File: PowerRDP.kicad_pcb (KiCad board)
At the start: 2 copper layers, 72.6 x 46.7 mm, 55 parts, among them J1 Conn_01x02_Male, J10 FPGA, J11 FAA LED, J12 Switch, J13 Conn_Coaxial, J14 Conn_Coaxial, J15 Conn_Coaxial, J2 Conn_01x02_Male, J3 Conn_01x02_Male, J4 Conn_01x02_Male, J5 Conn_01x02_Male, J6 Conn_01x02_Male, J7 3.3V, J8 5V, J9 12V, Q1 NTR4003NT1G, U1 Recom_RS3, U2 LM2575-3.3BU, U3 LM2575-5.0BU, U4 LM2575-12BU, U5 TS555, U6 MCP602, U7 MCP602

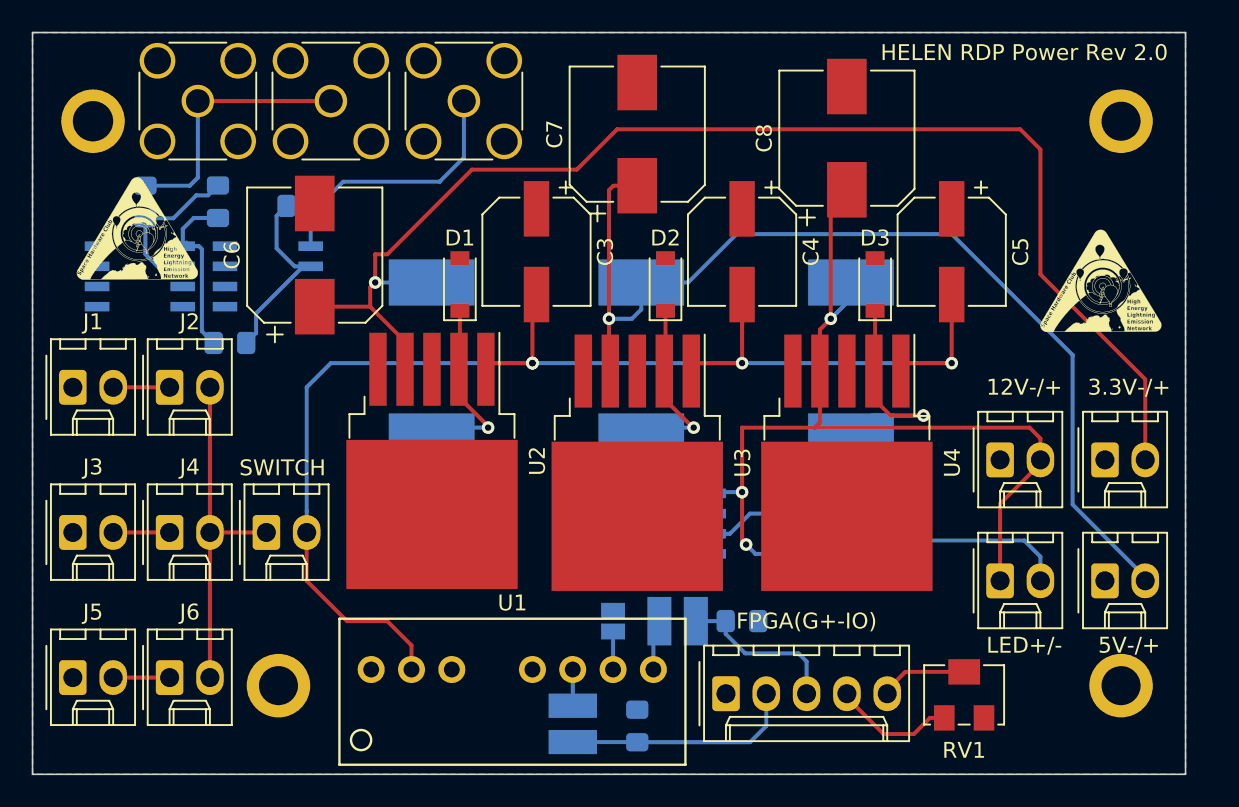
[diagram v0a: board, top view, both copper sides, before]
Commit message: Change R3 to through-hole for easier changes of amplification
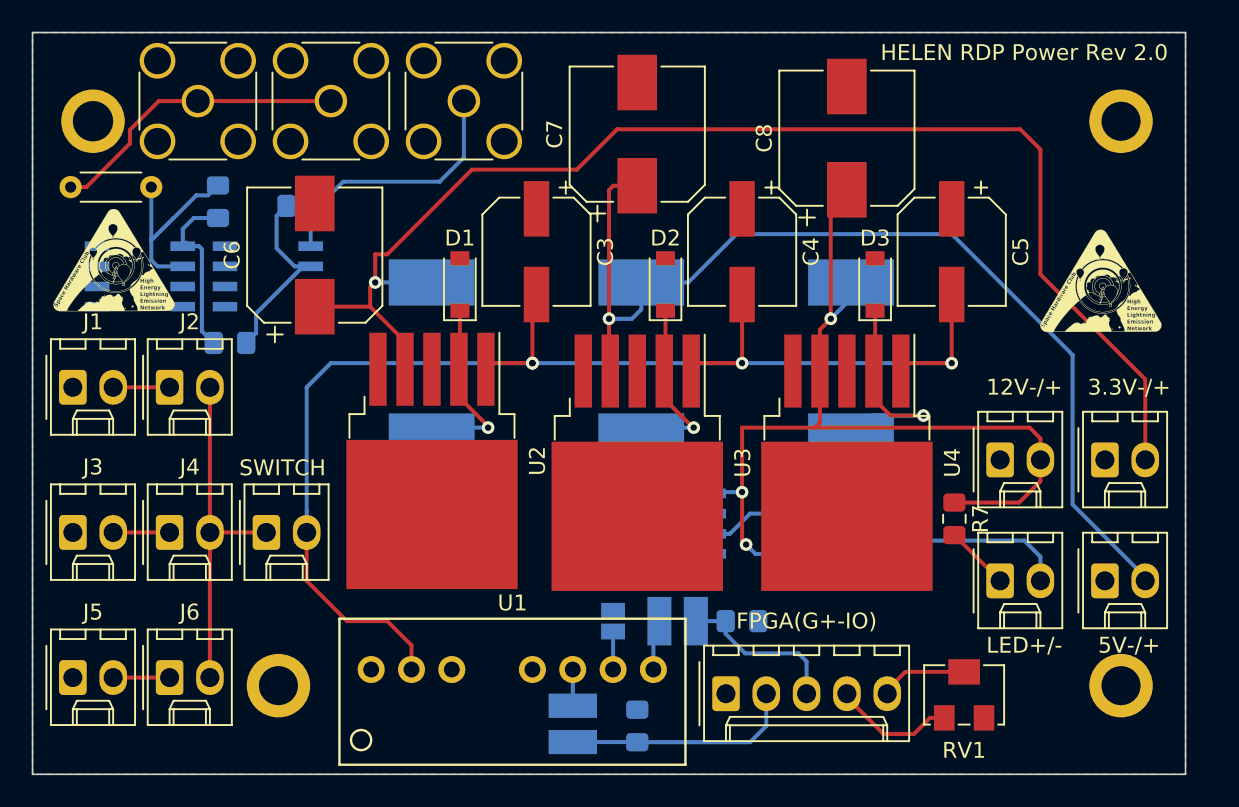
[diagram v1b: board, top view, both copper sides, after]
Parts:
- added R7: 15, Resistor_SMD:R_0805_2012Metric_Pad1.15x1.40mm_HandSolder, F.Cu at (141.9, 75.8)
- J10: value FPGA -> SOCKET
- R3: footprint Resistor_SMD:R_0805_2012Metric_Pad1.15x1.40mm_HandSolder -> Resistor_THT:R_Axial_DIN0204_L3.6mm_D1.6mm_P5.08mm_Horizontal; moved to F.Cu
- moved G*** 2.48 mm to (89.0, 59.4)
- moved R3 1.01 mm to (91.3, 55.0), turned to 180 degrees
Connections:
- J11 pad 1: /+12V -> Net-(J11-Pad1)
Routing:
- net Net-(J11-Pad1): track 0.00 -> 4.07 mm
- net /ADC1: track 16.7 -> 19.1 mm
- net Net-(R3-Pad1): track 11.1 -> 12.4 mm
- net /+12V: track 71.5 -> 70.4 mm

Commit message: Fix opamps
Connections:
- U6 pad 1: Net-(R4-Pad1) -> Net-(U6-Pad1)
- U6 pad 4: (no net) -> GND
- U6 pad 5: (no net) -> Net-(U6-Pad5)
- U6 pad 6: (no net) -> Net-(R4-Pad1)
- U6 pad 7: (no net) -> /+3.3V
- U6 pad 8: (no net) -> Net-(U6-Pad8)
- U7 pad 1: /ADC2 -> Net-(U7-Pad1)
- U7 pad 4: (no net) -> GND
- U7 pad 5: (no net) -> Net-(U7-Pad5)
- U7 pad 6: (no net) -> /ADC2
- U7 pad 7: (no net) -> /+3.3V
- U7 pad 8: (no net) -> Net-(U7-Pad8)
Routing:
- net /+3.3V: track 83.3 -> 103.0 mm, vias 1 -> 3
- net Net-(R4-Pad1): track 11.8 -> 25.1 mm, vias 0 -> 2
- net /ADC2: track 16.7 -> 27.6 mm
- net Net-(R3-Pad1): track 12.4 -> 11.4 mm
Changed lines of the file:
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@@
     (thickness 1.6)
     (drawings 24)
-    (tracks 209)
+    (tracks 231)
     (zones 0)
     (modules 56)
-    (nets 33)
+    (nets 39)
   )
   (page A4)
@@
   (net 31 "Net-(R5-Pad1)")
   (net 32 "Net-(J11-Pad1)")
+  (net 33 "Net-(U6-Pad8)")
+  (net 34 "Net-(U6-Pad5)")
+  (net 35 "Net-(U6-Pad1)")
+  (net 36 "Net-(U7-Pad1)")
+  (net 37 "Net-(U7-Pad5)")
+  (net 38 "Net-(U7-Pad8)")
   (net_class Default "This is the default net class."
     (clearance 0.2)
@@
     (add_net "Net-(U1-Pad3)")
     (add_net "Net-(U1-Pad5)")
+    (add_net "Net-(U6-Pad1)")
+    (add_net "Net-(U6-Pad5)")
+    (add_net "Net-(U6-Pad8)")
+    (add_net "Net-(U7-Pad1)")
+    (add_net "Net-(U7-Pad5)")
+    (add_net "Net-(U7-Pad8)")
   )
   (module rdplibs:HELENlogo_large (layer F.Cu)
@@
       (effects (font (size 1 1) (thickness 0.15)) (justify mirror))
     )
-    (pad 8 smd rect (at 2.7 1.905 180) (size 1.55 0.6) (layers B.Cu B.Paste B.Mask))
-    (pad 7 smd rect (at 2.7 0.635 180) (size 1.55 0.6) (layers B.Cu B.Paste B.Mask))
-    (pad 6 smd rect (at 2.7 -0.635 180) (size 1.55 0.6) (layers B.Cu B.Paste B.Mask))
-    (pad 5 smd rect (at 2.7 -1.905 180) (size 1.55 0.6) (layers B.Cu B.Paste B.Mask))
-    (pad 4 smd rect (at -2.7 -1.905 180) (size 1.55 0.6) (layers B.Cu B.Paste B.Mask))
+    (pad 8 smd rect (at 2.7 1.905 180) (size 1.55 0.6) (layers B.Cu B.Paste B.Mask)
+      (net 33 "Net-(U6-Pad8)"))
+    (pad 7 smd rect (at 2.7 0.635 180) (size 1.55 0.6) (layers B.Cu B.Paste B.Mask)
+      (net 5 /+3.3V))
+    (pad 6 smd rect (at 2.7 -0.635 180) (size 1.55 0.6) (layers B.Cu B.Paste B.Mask)
+      (net 30 "Net-(R4-Pad1)"))
+    (pad 5 smd rect (at 2.7 -1.905 180) (size 1.55 0.6) (layers B.Cu B.Paste B.Mask)
+      (net 34 "Net-(U6-Pad5)"))
+    (pad 4 smd rect (at -2.7 -1.905 180) (size 1.55 0.6) (layers B.Cu B.Paste B.Mask)
+      (net 2 GND))
     (pad 3 smd rect (at -2.7 -0.635 180) (size 1.55 0.6) (layers B.Cu B.Paste B.Mask)
       (net 2 GND))
@@
       (net 29 "Net-(R3-Pad1)"))
     (pad 1 smd rect (at -2.7 1.905 180) (size 1.55 0.6) (layers B.Cu B.Paste B.Mask)
-      (net 30 "Net-(R4-Pad1)"))
+      (net 35 "Net-(U6-Pad1)"))
     (model ${KISYS3DMOD}/Package_SO.3dshapes/SOIC-8_3.9x4.9mm_P1.27mm.wrl
       (at (xyz 0 0 0))
@@
     (fp_line (start -2.075 2.525) (end -3.475 2.525) (layer B.SilkS) (width 0.15))
     (pad 1 smd rect (at -2.7 1.905 180) (size 1.55 0.6) (layers B.Cu B.Paste B.Mask)
-      (net 28 /ADC2))
+      (net 36 "Net-(U7-Pad1)"))
     (pad 2 smd rect (at -2.7 0.635 180) (size 1.55 0.6) (layers B.Cu B.Paste B.Mask)
       (net 31 "Net-(R5-Pad1)"))
     (pad 3 smd rect (at -2.7 -0.635 180) (size 1.55 0.6) (layers B.Cu B.Paste B.Mask)
       (net 2 GND))
-    (pad 4 smd rect (at -2.7 -1.905 180) (size 1.55 0.6) (layers B.Cu B.Paste B.Mask))
-    (pad 5 smd rect (at 2.7 -1.905 180) (size 1.55 0.6) (layers B.Cu B.Paste B.Mask))
-    (pad 6 smd rect (at 2.7 -0.635 180) (size 1.55 0.6) (layers B.Cu B.Paste B.Mask))
-    (pad 7 smd rect (at 2.7 0.635 180) (size 1.55 0.6) (layers B.Cu B.Paste B.Mask))
-    (pad 8 smd rect (at 2.7 1.905 180) (size 1.55 0.6) (layers B.Cu B.Paste B.Mask))
+    (pad 4 smd rect (at -2.7 -1.905 180) (size 1.55 0.6) (layers B.Cu B.Paste B.Mask)
+      (net 2 GND))
+    (pad 5 smd rect (at 2.7 -1.905 180) (size 1.55 0.6) (layers B.Cu B.Paste B.Mask)
+      (net 37 "Net-(U7-Pad5)"))
+    (pad 6 smd rect (at 2.7 -0.635 180) (size 1.55 0.6) (layers B.Cu B.Paste B.Mask)
+      (net 28 /ADC2))
+    (pad 7 smd rect (at 2.7 0.635 180) (size 1.55 0.6) (layers B.Cu B.Paste B.Mask)
+      (net 5 /+3.3V))
+    (pad 8 smd rect (at 2.7 1.905 180) (size 1.55 0.6) (layers B.Cu B.Paste B.Mask)
+      (net 38 "Net-(U7-Pad8)"))
     (model ${KISYS3DMOD}/Package_SO.3dshapes/SOIC-8_3.9x4.9mm_P1.27mm.wrl
       (at (xyz 0 0 0))
@@
   (segment (start 120.65 51.308) (end 146.05 51.308) (width 0.25) (layer F.Cu) (net 5))
   (segment (start 118.11 53.848) (end 120.65 51.308) (width 0.25) (layer F.Cu) (net 5))
+  (via (at 97.79 59.944) (size 0.8) (drill 0.4) (layers F.Cu B.Cu) (net 5))
+  (segment (start 101.6 62.484) (end 101.6 61.984) (width 0.25) (layer F.Cu) (net 5))
+  (segment (start 99.56 59.944) (end 97.79 59.944) (width 0.25) (layer F.Cu) (net 5))
+  (segment (start 101.6 61.984) (end 99.56 59.944) (width 0.25) (layer F.Cu) (net 5))
+  (segment (start 97.79 59.944) (end 95.946 59.944) (width 0.25) (layer B.Cu) (net 5))
+  (segment (start 97.79 59.944) (end 93.218 59.944) (width 0.25) (layer F.Cu) (net 5))
+  (via (at 90.424 57.15) (size 0.8) (drill 0.4) (layers F.Cu B.Cu) (net 5))
+  (segment (start 93.218 59.944) (end 90.424 57.15) (width 0.25) (layer F.Cu) (net 5))
+  (segment (start 88.359 59.944) (end 87.884 59.944) (width 0.25) (layer B.Cu) (net 5))
+  (segment (start 90.424 57.879) (end 88.359 59.944) (width 0.25) (layer B.Cu) (net 5))
+  (segment (start 90.424 57.15) (end 90.424 57.879) (width 0.25) (layer B.Cu) (net 5))
   (segment (start 120.22 66.542) (end 120.22 68.292) (width 0.25) (layer F.Cu) (net 6))
   (via (at 120.142 63.246) (size 0.8) (drill 0.4) (layers F.Cu B.Cu) (net 6))
@@
   (segment (start 87.209949 54.95) (end 86.22 54.95) (width 0.25) (layer F.Cu) (net 27))
   (segment (start 91.77 49.53) (end 89.955001 51.344999) (width 0.25) (layer F.Cu) (net 27))
-  (segment (start 101.346 56.66) (end 101.872 56.134) (width 0.25) (layer B.Cu) (net 28))
-  (segment (start 101.346 58.674) (end 101.346 56.66) (width 0.25) (layer B.Cu) (net 28))
   (segment (start 103.396 54.61) (end 101.872 56.134) (width 0.25) (layer B.Cu) (net 28))
   (segment (start 109.474 54.61) (end 103.396 54.61) (width 0.25) (layer B.Cu) (net 28))
   (segment (start 110.998 49.53) (end 110.998 53.086) (width 0.25) (layer B.Cu) (net 28))
   (segment (start 110.998 53.086) (end 109.474 54.61) (width 0.25) (layer B.Cu) (net 28))
+  (segment (start 100.094 54.356) (end 101.872 56.134) (width 0.25) (layer B.Cu) (net 28))
+  (segment (start 98.552 54.356) (end 100.094 54.356) (width 0.25) (layer B.Cu) (net 28))
+  (segment (start 98.044 61.214) (end 98.806 60.452) (width 0.25) (layer B.Cu) (net 28))
+  (segment (start 98.298 54.61) (end 98.552 54.356) (width 0.25) (layer B.Cu) (net 28))
+  (segment (start 95.946 61.214) (end 98.044 61.214) (width 0.25) (layer B.Cu) (net 28))
+  (segment (start 98.806 60.452) (end 98.806 59.69) (width 0.25) (layer B.Cu) (net 28))
+  (segment (start 98.806 59.69) (end 98.298 59.182) (width 0.25) (layer B.Cu) (net 28))
+  (segment (start 98.298 59.182) (end 98.298 54.61) (width 0.25) (layer B.Cu) (net 28))
   (segment (start 94.880628 55.469372) (end 94.136628 55.469372) (width 0.25) (layer B.Cu) (net 29))
   (segment (start 95.504 54.846) (end 94.880628 55.469372) (width 0.25) (layer B.Cu) (net 29))
-  (segment (start 94.136628 55.469372) (end 92.692 56.914) (width 0.25) (layer B.Cu) (net 29))
   (segment (start 91.694 59.944) (end 93.284 59.944) (width 0.25) (layer B.Cu) (net 29))
   (segment (start 91.3 59.55) (end 91.694 59.944) (width 0.25) (layer B.Cu) (net 29))
-  (segment (start 92.686 56.914) (end 91.3 58.3) (width 0.25) (layer B.Cu) (net 29))
-  (segment (start 92.692 56.914) (end 92.686 56.914) (width 0.25) (layer B.Cu) (net 29))
   (segment (start 91.3 54.95) (end 91.3 58.3) (width 0.25) (layer B.Cu) (net 29))
   (segment (start 91.3 58.3) (end 91.3 59.55) (width 0.25) (layer B.Cu) (net 29))
-  (segment (start 93.52 58.438) (end 93.284 58.674) (width 0.25) (layer B.Cu) (net 30))
+  (segment (start 93.617256 54.95) (end 91.3 54.95) (width 0.25) (layer B.Cu) (net 29))
+  (segment (start 94.136628 55.469372) (end 93.617256 54.95) (width 0.25) (layer B.Cu) (net 29))
   (segment (start 95.504 64.498) (end 95.232 64.77) (width 0.25) (layer B.Cu) (net 30))
-  (segment (start 93.284 57.592) (end 93.284 58.674) (width 0.25) (layer B.Cu) (net 30))
   (segment (start 95.504 56.896) (end 93.98 56.896) (width 0.25) (layer B.Cu) (net 30))
-  (segment (start 93.98 56.896) (end 93.284 57.592) (width 0.25) (layer B.Cu) (net 30))
-  (segment (start 94.309 58.674) (end 94.488 58.853) (width 0.25) (layer B.Cu) (net 30))
-  (segment (start 93.284 58.674) (end 94.309 58.674) (width 0.25) (layer B.Cu) (net 30))
-  (segment (start 94.488 64.026) (end 95.232 64.77) (width 0.25) (layer B.Cu) (net 30))
-  (segment (start 94.488 58.853) (end 94.488 64.026) (width 0.25) (layer B.Cu) (net 30))
+  (segment (start 86.859 61.214) (end 85.852 60.207) (width 0.25) (layer B.Cu) (net 30))
+  (segment (start 87.884 61.214) (end 86.859 61.214) (width 0.25) (layer B.Cu) (net 30))
+  (segment (start 85.852 60.207) (end 85.852 56.642) (width 0.25) (layer B.Cu) (net 30))
+  (via (at 85.852 56.642) (size 0.8) (drill 0.4) (layers F.Cu B.Cu) (net 30))
+  (via (at 92.964 56.642) (size 0.8) (drill 0.4) (layers F.Cu B.Cu) (net 30))
+  (segment (start 92.564001 56.242001) (end 92.964 56.642) (width 0.25) (layer F.Cu) (net 30))
+  (segment (start 85.852 56.642) (end 86.251999 56.242001) (width 0.25) (layer F.Cu) (net 30))
+  (segment (start 86.251999 56.242001) (end 92.564001 56.242001) (width 0.25) (layer F.Cu) (net 30))
+  (segment (start 93.726 56.642) (end 92.964 56.642) (width 0.25) (layer B.Cu) (net 30))
+  (segment (start 93.98 56.896) (end 93.726 56.642) (width 0.25) (layer B.Cu) (net 30))
+  (segment (start 94.488 57.912) (end 95.504 56.896) (width 0.25) (layer B.Cu) (net 30))
+  (segment (start 95.232 64.77) (end 94.488 64.026) (width 0.25) (layer B.Cu) (net 30))
+  (segment (start 94.488 64.026) (end 94.488 57.912) (width 0.25) (layer B.Cu) (net 30))
   (segment (start 100.871 59.944) (end 101.346 59.944) (width 0.25) (layer B.Cu) (net 31))
   (segment (start 97.905372 62.909628) (end 100.871 59.944) (width 0.25) (layer B.Cu) (net 31))

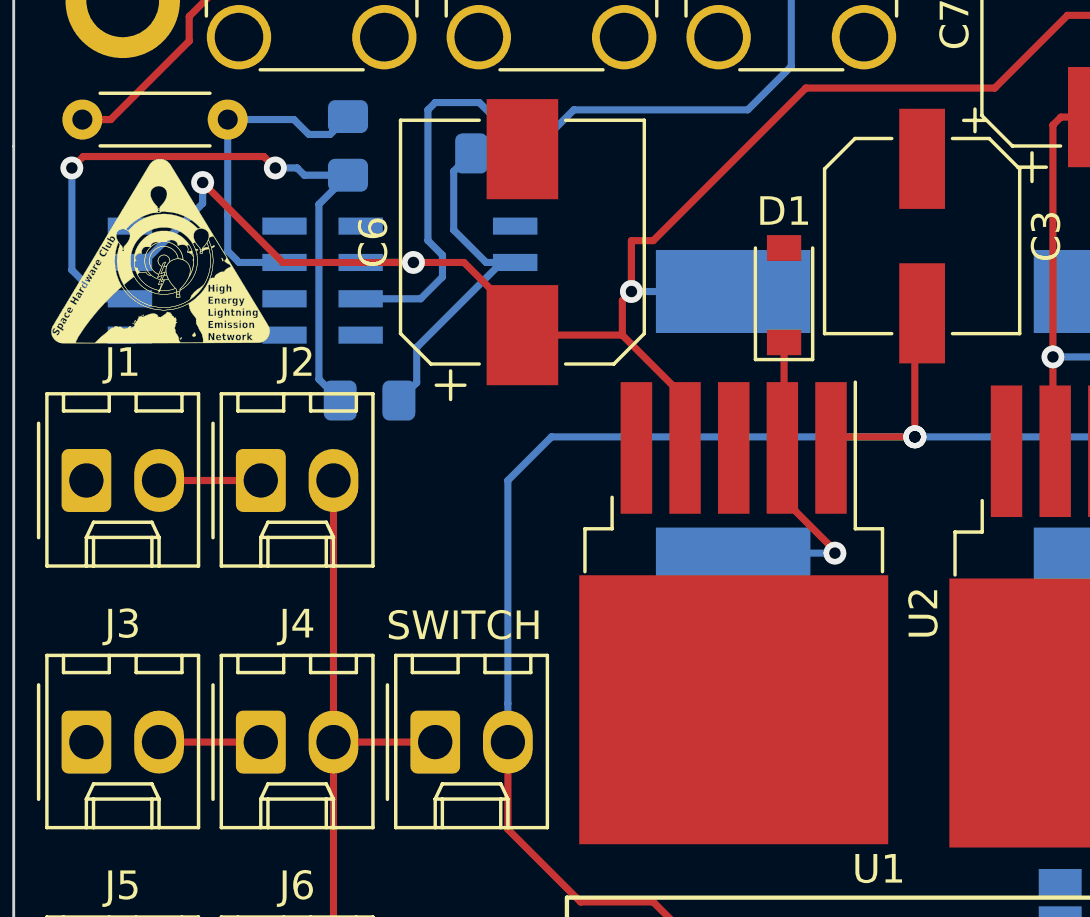
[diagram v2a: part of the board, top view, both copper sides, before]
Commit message: Fix opamps by adding -V supply
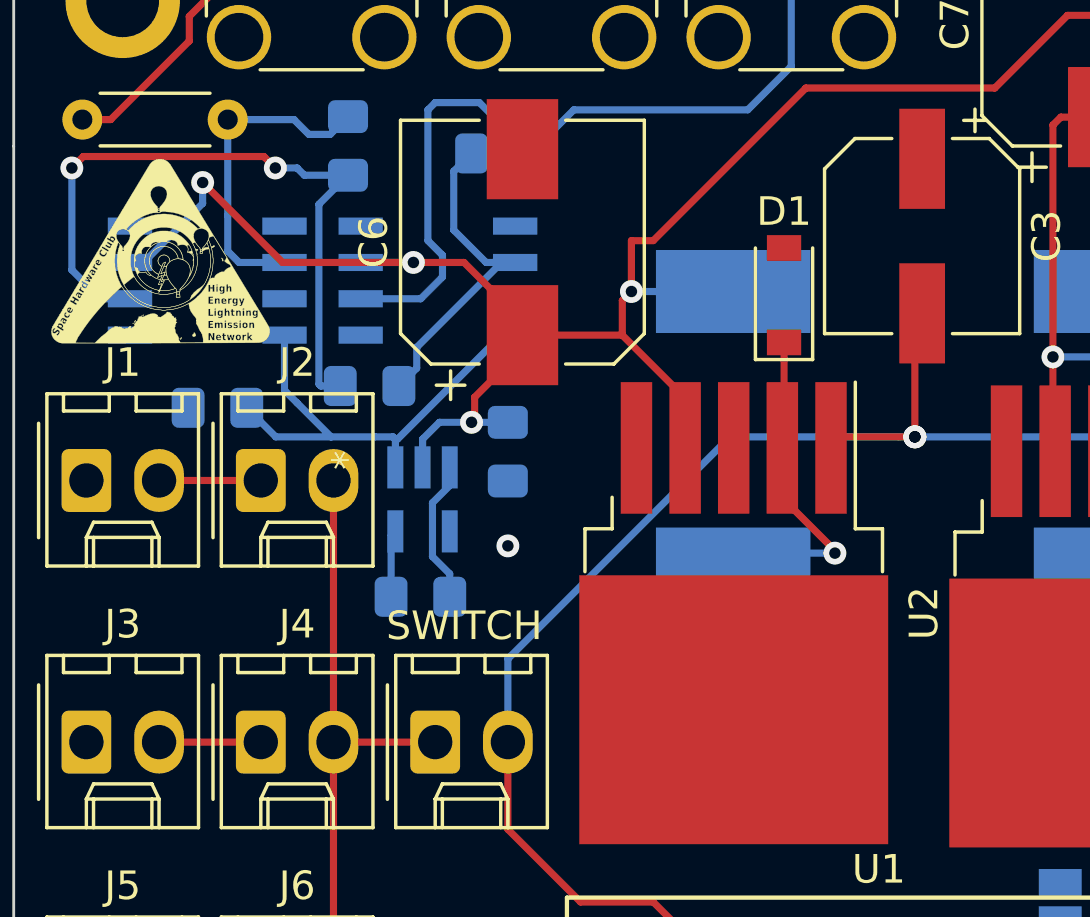
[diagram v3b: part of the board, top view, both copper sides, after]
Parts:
- added C11: 1uF, Capacitor_SMD:C_0805_2012Metric_Pad1.15x1.40mm_HandSolder, B.Cu at (90.9, 65.0)
- added C12: 1uF, Capacitor_SMD:C_0805_2012Metric_Pad1.15x1.40mm_HandSolder, B.Cu at (101.1, 66.6)
- added C13: 1uF, Capacitor_SMD:C_0805_2012Metric_Pad1.15x1.40mm_HandSolder, B.Cu at (98.0, 71.6)
- added U8: TPS60400DBVR, footprints:TPS60400DBVR, B.Cu at (98.1, 68.2)
- moved R5 0.51 mm to (96.3, 64.3)
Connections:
- U6 pad 4: GND -> /-3.3V
- U7 pad 4: GND -> /-3.3V
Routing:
- net /-3.3V: track 0.00 -> 16.6 mm
- net /+3.3V: track 103.0 -> 111.0 mm, vias 3 -> 4
- net Net-(C13-Pad2): track 0.00 -> 5.02 mm
- net /POWR: track 86.2 -> 82.6 mm
- net Net-(C13-Pad1): track 0.00 -> 2.35 mm
- net Net-(R5-Pad1): track 12.3 -> 11.8 mm
- net GND: vias 0 -> 1
